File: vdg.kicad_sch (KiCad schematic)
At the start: 3 parts, among them IC12 MC6847, IC13 74LS273

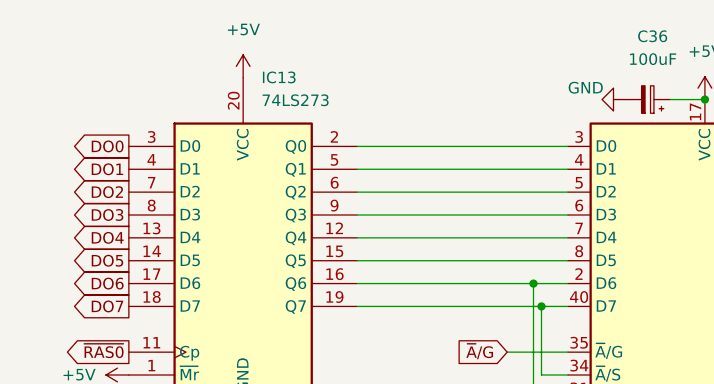
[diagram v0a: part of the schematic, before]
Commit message: cross-reference items to suppliers
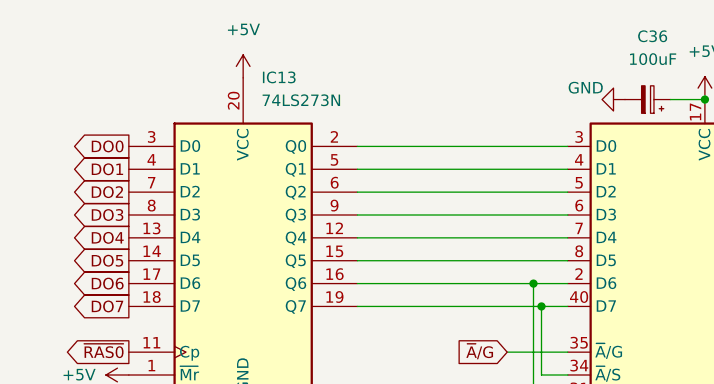
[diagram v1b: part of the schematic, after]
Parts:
- IC13: value 74LS273 -> 74LS273N
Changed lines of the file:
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@@
       (effects (font (size 1.27 1.27)) (justify left))
     )
-    (property "Value" "74LS273" (id 1) (at 113.2714 65.532 0)
+    (property "Value" "74LS273N" (id 1) (at 113.2714 65.532 0)
       (effects (font (size 1.27 1.27)) (justify left))
     )

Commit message: update part numbers
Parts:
- C36: footprint Capacitor_THT:CP_Radial_D7.5mm_P2.50mm -> Capacitor_THT:CP_Radial_D6.3mm_P2.50mm; DigiKey (none) -> 732-8598-1-ND
- IC12: Note (none) -> donor
- IC13: DigiKey (none) -> 296-1657-5-ND
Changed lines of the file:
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@@
+      (effects (font (size 1.27 1.27)) hide)
+    )
+    (property "Note" "" (id 4) (at 111.252 83.312 0)
+      (effects (font (size 1.27 1.27)) hide)
+    )
+    (property "DigiKey" "296-1657-5-ND" (id 5) (at 111.252 83.312 0)
       (effects (font (size 1.27 1.27)) hide)
     )
@@
     (property "Reference" "C36" (id 0) (at 156.7561 58.42 90))
     (property "Value" "100uF" (id 1) (at 156.7561 60.96 90))
-    (property "Footprint" "Capacitor_THT:CP_Radial_D7.5mm_P2.50mm" (id 2) (at 156.21 65.405 0)
+    (property "Footprint" "Capacitor_THT:CP_Radial_D6.3mm_P2.50mm" (id 2) (at 156.21 65.405 0)
       (effects (font (size 1.27 1.27)) hide)
     )
-    (property "Datasheet" "~" (id 3) (at 156.21 65.405 0)
+    (property "Datasheet" "https://www.we-online.com/katalog/datasheet/860010372006.pdf" (id 3) (at 156.21 65.405 0)
+      (effects (font (size 1.27 1.27)) hide)
+    )
+    (property "DigiKey" "732-8598-1-ND" (id 4) (at 156.21 65.405 0)
       (effects (font (size 1.27 1.27)) hide)
     )
@@
       (effects (font (size 1.27 1.27)) hide)
     )
+    (property "Note" "donor" (id 4) (at 162.56 101.092 0)
+      (effects (font (size 1.27 1.27)) hide)
+    )
